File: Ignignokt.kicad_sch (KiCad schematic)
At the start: 270 parts, among them J1 Barrel_Jack_Switch, J2 Conn_01x02_Pin, Q1 IRLB8721PBF, Q2 FQP27P06, U1 LM2585S-12, U2 LM2937ET-5.0, U3 PIC12F675-IMC

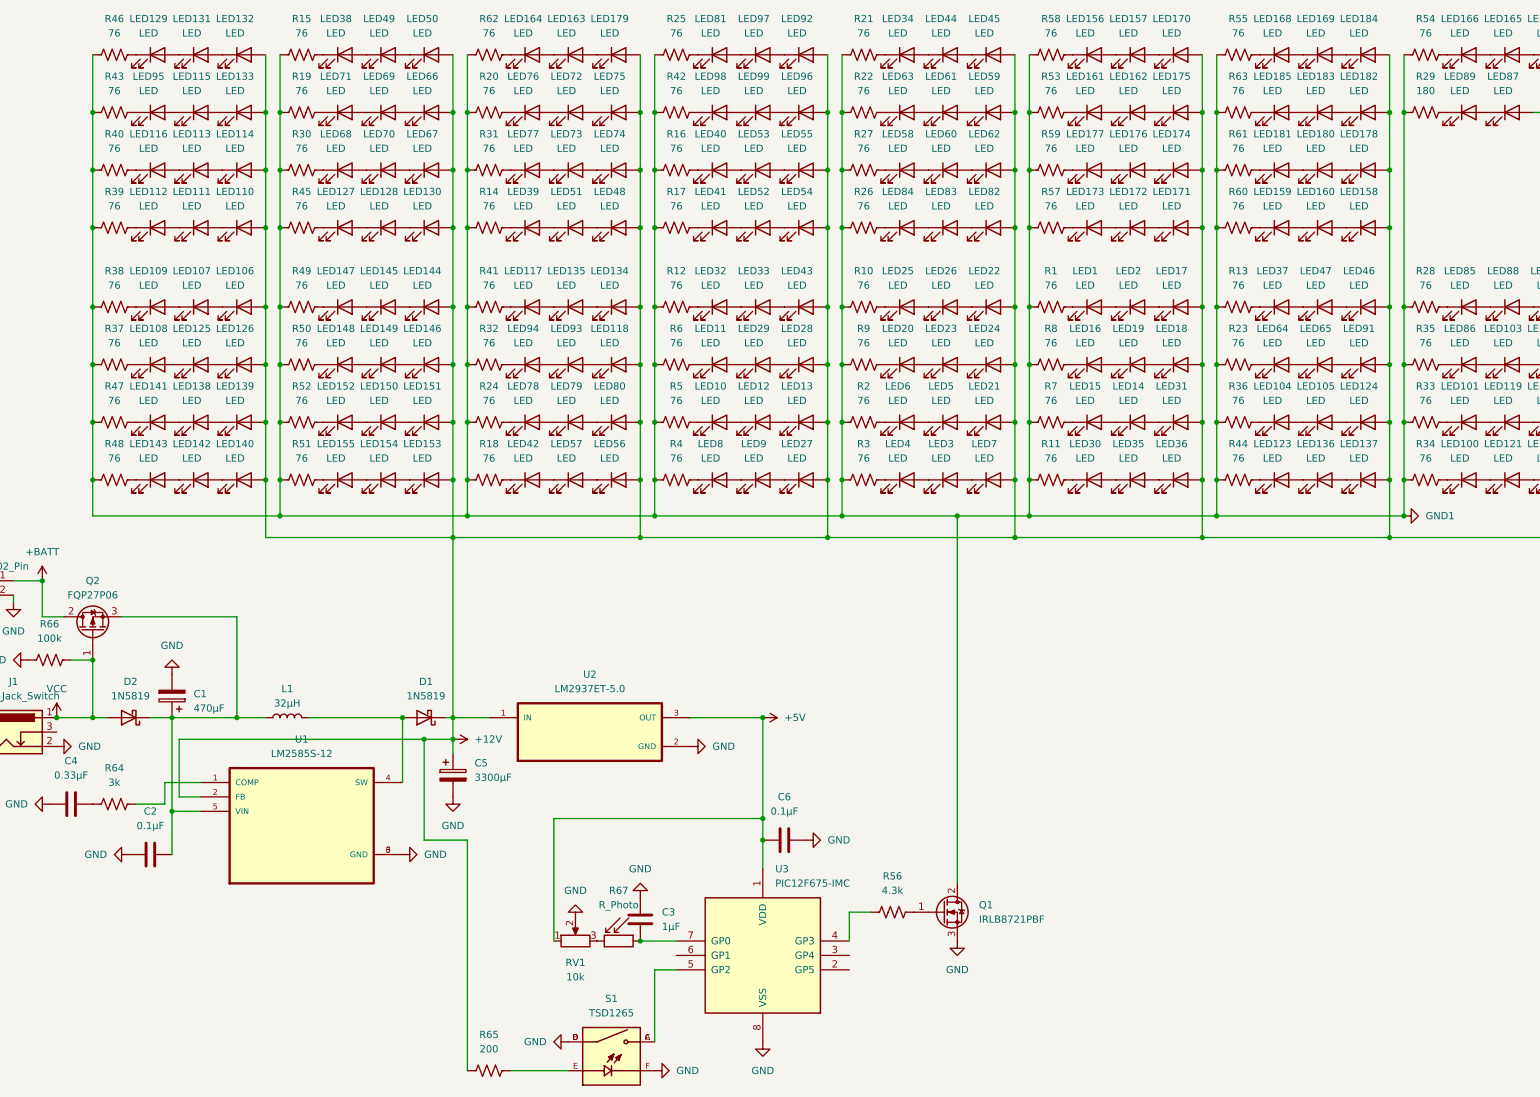
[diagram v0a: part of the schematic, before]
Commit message: Small tweaks to board
The MOSFET for the LEDs was a TO-247 which did not match the part I had selected. Changed it to a TO-220 to match the part. Also added a pull-down resistor to the gate to ensure it turns off when there is no longer a voltage on the pin. The PIC chip will ground it but it makes sense to have the extra part in case the board is used without it.

Signed-off-by: Nathan Hjelm <hjelmn@me.com>
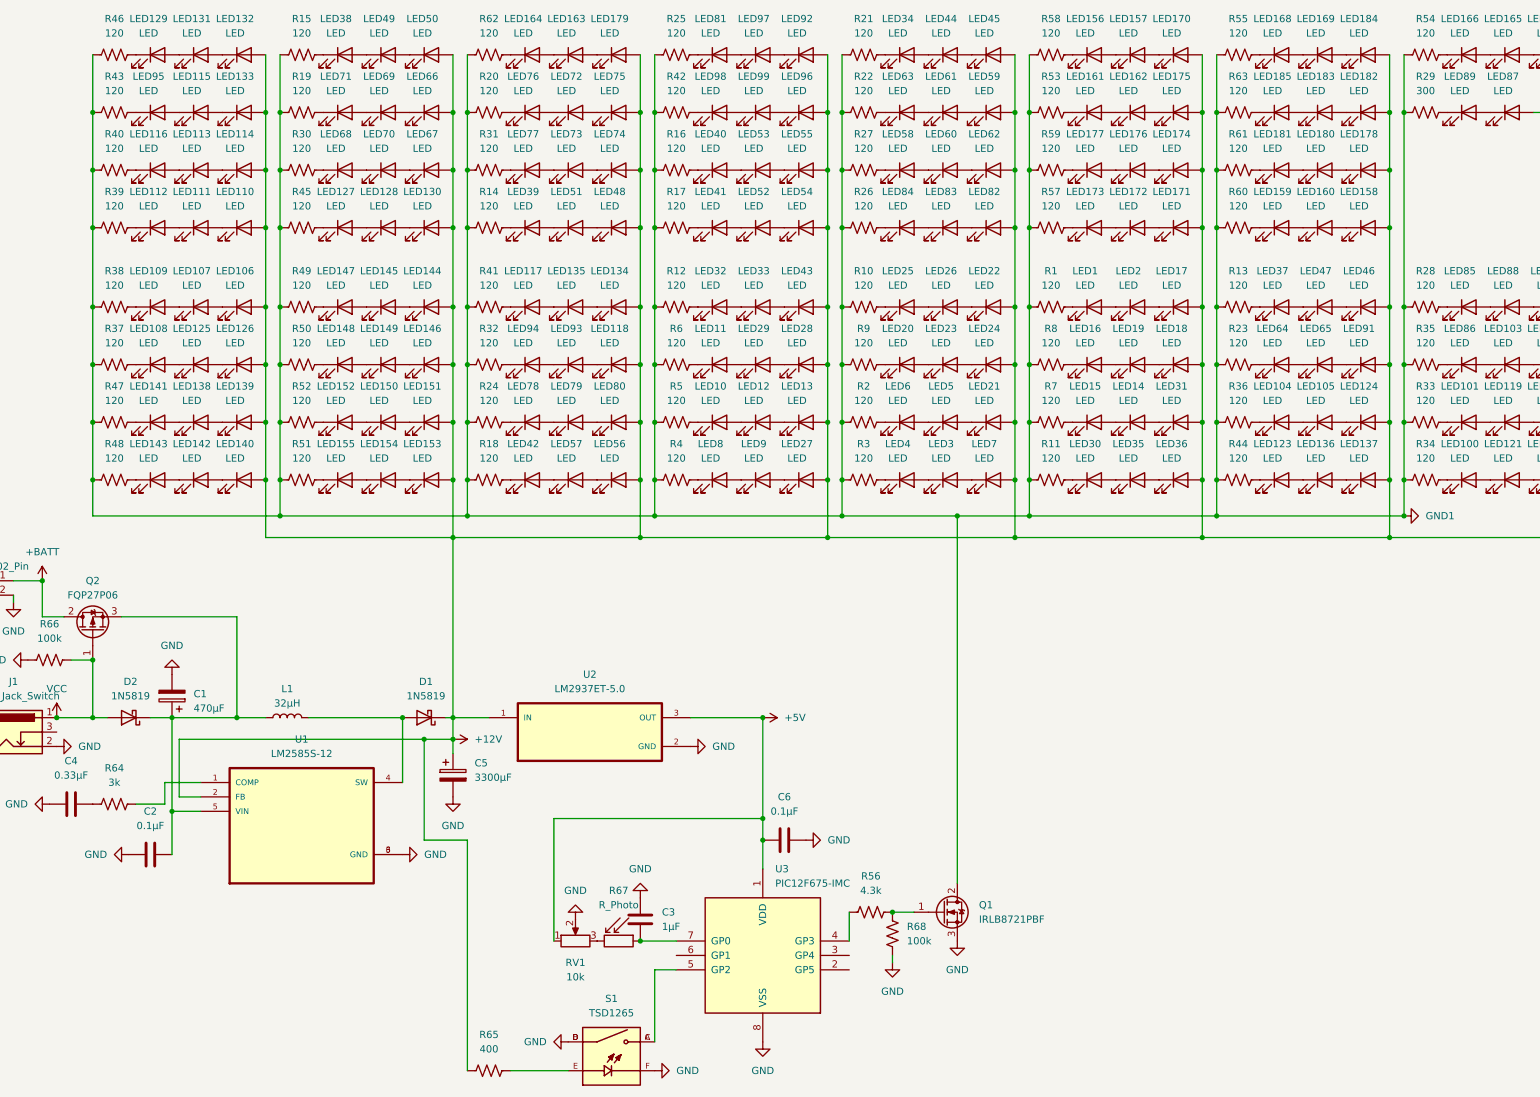
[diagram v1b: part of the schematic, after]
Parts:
- added R68: 100k, Resistor_THT:R_Axial_DIN0207_L6.3mm_D2.5mm_P10.16mm_Horizontal, symbol Device:R_US
- Q1: footprint Package_TO_SOT_THT:TO-247-3_Vertical -> Package_TO_SOT_THT:TO-220-3_Vertical
- R1, R10, R11, R12, R13, R14, R15, R16, R17, R18, R19, R2, R20, R21, R22, R23, R24, R25, R26, R27, R28, R3, R30, R31, R32, R33, R34, R35, R36, R37, R38, R39, R4, R40, R41, R42, R43, R44, R45, R46, R47, R48, R49, R5, R50, R51, R52, R53, R54, R55, R57, R58, R59, R6, R60, R61, R62, R63, R7, R8, R9: value 76 -> 120
- R29: value 180 -> 300
- R65: value 200 -> 400
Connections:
- net GND: now also R68.2
- net at Q1.1 (G), R56.1: now also R68.1
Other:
- moved on the sheet: R56

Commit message: Small tweaks
The original schematic I used to design the board erroneously used pin 4 (GPIO3) as an output pin. This will not work with a PIC2F675 as that pin is input-only. Moved the output to GPIO4 to correct the issue and adjusted some other components based on observations.

To fix the boards I have I put a jumper between GPIO3 and GPIO4 and disabled external MCLR to avoid the output causing a reset of the chip.

Also, can use a 200 ohm resistor in place of the potentiometer (dropped to 1k). 10k might be a bit too high but could work as well. Will do more calculations to see what is best since the 10k can only go down to 5.3k. At 200 ohm it takes about 8 clock cycles for the GPIO pin to register high at the appropriate light level.

Signed-off-by: Nathan Hjelm <hjelmn@me.com>
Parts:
- removed R68: 100k, Resistor_THT:R_Axial_DIN0207_L6.3mm_D2.5mm_P10.16mm_Horizontal, symbol Device:R_US
- added C7: 1µF, Capacitor_THT:C_Disc_D5.1mm_W3.2mm_P5.00mm, symbol Device:C
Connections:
- net GND: now also C7.2
- net at U3.3 (GP4): now also R56.2
- net at U3.4 (GP3): no longer R56.2
- net at S1.A, S1.C, U3.5 (GP2): now also C7.1
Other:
- moved on the sheet: R56
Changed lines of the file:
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@@
   (junction (at 284.48 66.04) (diameter 0) (color 0 0 0 0)
   )
-  (junction (at 194.31 172.72) (diameter 0) (color 0 0 0 0)
-  )
   (junction (at 182.88 41.91) (diameter 0) (color 0 0 0 0)
   )
@@
   (junction (at 67.31 154.94) (diameter 0) (color 0 0 0 0)
   )
+  (junction (at 152.4 182.88) (diameter 0) (color 0 0 0 0)
+  )
   (junction (at 314.96 31.75) (diameter 0) (color 0 0 0 0)
   )
@@
     (stroke (width 0) (type default))
   )
-  (wire (pts (xy 186.69 172.72) (xy 186.69 177.8))
-    (stroke (width 0) (type default))
-  )
   (wire (pts (xy 205.74 102.87) (xy 185.42 102.87))
     (stroke (width 0) (type default))
@@
     (stroke (width 0) (type default))
   )
+  (wire (pts (xy 186.69 180.34) (xy 189.23 180.34))
+    (stroke (width 0) (type default))
+  )
   (wire (pts (xy 119.38 86.36) (xy 119.38 96.52))
     (stroke (width 0) (type default))
@@
     (stroke (width 0) (type default))
   )
-  (wire (pts (xy 194.31 172.72) (xy 198.12 172.72))
+  (wire (pts (xy 189.23 172.72) (xy 198.12 172.72))
     (stroke (width 0) (type default))
   )
@@
     (stroke (width 0) (type default))
   )
-  (wire (pts (xy 194.31 180.34) (xy 194.31 181.61))
-    (stroke (width 0) (type default))
-  )
   (wire (pts (xy 156.21 182.88) (xy 152.4 182.88))
     (stroke (width 0) (type default))
@@
     )
   )
+  (symbol (lib_id "Device:C") (at 148.59 182.88 270) (unit 1)
+    (in_bom yes) (on_board yes) (dnp no) (fields_autoplaced)
+    (property "Reference" "C7" (at 148.59 175.26 90)
+      (effects (font (size 1.27 1.27)))
+    )
+    (property "Value" "1µF" (at 148.59 177.8 90)
+      (effects (font (size 1.27 1.27)))
+    )
+    (property "Footprint" "Capacitor_THT:C_Disc_D5.1mm_W3.2mm_P5.00mm" (at 144.78 183.8452 0)
+      (effects (font (size 1.27 1.27)) hide)
+    )
+    (property "Datasheet" "~" (at 148.59 182.88 0)
+      (effects (font (size 1.27 1.27)) hide)
+    )
+    (pin "2")
+    (pin "1")
+    (instances
+      (project "Ignignokt"
+        (path "/f0a33db0-88ba-4d3e-9175-b5a39f1c39d8"
+          (reference "C7") (unit 1)
+        )
+      )
+    )
+  )
   (symbol (lib_id "Device:R_US") (at 156.21 31.75 270) (unit 1)
     (in_bom yes) (on_board yes) (dnp no) (fields_autoplaced)
@@
     )
   )
-  (symbol (lib_id "Device:R_US") (at 194.31 176.53 0) (unit 1)
-    (in_bom yes) (on_board yes) (dnp no) (fields_autoplaced)
-    (property "Reference" "R68" (at 196.85 175.26 0)
-      (effects (font (size 1.27 1.27)) (justify left))
-    )
-    (property "Value" "100k" (at 196.85 177.8 0)
-      (effects (font (size 1.27 1.27)) (justify left))
-    )
-    (property "Footprint" "Resistor_THT:R_Axial_DIN0207_L6.3mm_D2.5mm_P10.16mm_Horizontal" (at 195.326 176.784 90)
-      (effects (font (size 1.27 1.27)) hide)
-    )
-    (property "Datasheet" "~" (at 194.31 176.53 0)
-      (effects (font (size 1.27 1.27)) hide)
-    )
-    (pin "1")
-    (pin "2")
-    (instances
-      (project "Ignignokt"
-        (path "/f0a33db0-88ba-4d3e-9175-b5a39f1c39d8"
-          (reference "R68") (unit 1)
-        )
-      )
-    )
-  )
   (symbol (lib_id "Device:LED") (at 212.09 66.04 0) (unit 1)
     (in_bom yes) (on_board yes) (dnp no) (fields_autoplaced)
@@
     )
   )
-  (symbol (lib_id "power:GND") (at 194.31 181.61 0) (unit 1)
-    (in_bom yes) (on_board yes) (dnp no) (fields_autoplaced)
-    (property "Reference" "#PWR022" (at 194.31 187.96 0)
-      (effects (font (size 1.27 1.27)) hide)
-    )
-    (property "Value" "GND" (at 194.31 186.69 0)
-      (effects (font (size 1.27 1.27)))
-    )
-    (property "Footprint" "" (at 194.31 181.61 0)
-      (effects (font (size 1.27 1.27)) hide)
-    )
-    (property "Datasheet" "" (at 194.31 181.61 0)
-      (effects (font (size 1.27 1.27)) hide)
-    )
-    (pin "1")
-    (instances
-      (project "Ignignokt"
-        (path "/f0a33db0-88ba-4d3e-9175-b5a39f1c39d8"
-          (reference "#PWR022") (unit 1)
-        )
-      )
-    )
-  )
   (symbol (lib_id "Device:R_US") (at 222.25 31.75 270) (unit 1)
     (in_bom yes) (on_board yes) (dnp no) (fields_autoplaced)
@@
     )
   )
-  (symbol (lib_id "Device:R_US") (at 190.5 172.72 270) (unit 1)
+  (symbol (lib_id "Device:R_US") (at 189.23 176.53 0) (unit 1)
     (in_bom yes) (on_board yes) (dnp no) (fields_autoplaced)
-    (property "Reference" "R56" (at 190.5 166.37 90)
-      (effects (font (size 1.27 1.27)))
+    (property "Reference" "R56" (at 191.77 175.26 0)
+      (effects (font (size 1.27 1.27)) (justify left))
     )
-    (property "Value" "4.3k" (at 190.5 168.91 90)
-      (effects (font (size 1.27 1.27)))
+    (property "Value" "4.3k" (at 191.77 177.8 0)
+      (effects (font (size 1.27 1.27)) (justify left))
     )
-    (property "Footprint" "Resistor_THT:R_Axial_DIN0207_L6.3mm_D2.5mm_P10.16mm_Horizontal" (at 190.246 173.736 90)
+    (property "Footprint" "Resistor_THT:R_Axial_DIN0207_L6.3mm_D2.5mm_P10.16mm_Horizontal" (at 190.246 176.784 90)
       (effects (font (size 1.27 1.27)) hide)
     )
-    (property "Datasheet" "~" (at 190.5 172.72 0)
+    (property "Datasheet" "~" (at 189.23 176.53 0)
       (effects (font (size 1.27 1.27)) hide)
     )
@@
         )
       )
+    )
+  )
+  (symbol (lib_id "power:GND") (at 144.78 182.88 270) (unit 1)
+    (in_bom yes) (on_board yes) (dnp no) (fields_autoplaced)
+    (property "Reference" "#PWR023" (at 138.43 182.88 0)
+      (effects (font (size 1.27 1.27)) hide)
+    )
+    (property "Value" "GND" (at 140.97 182.88 90)
+      (effects (font (size 1.27 1.27)) (justify right))
+    )
+    (property "Footprint" "" (at 144.78 182.88 0)
+      (effects (font (size 1.27 1.27)) hide)
+    )
+    (property "Datasheet" "" (at 144.78 182.88 0)
+      (effects (font (size 1.27 1.27)) hide)
+    )
+    (pin "1")
+    (instances
+      (project "Ignignokt"
+        (path "/f0a33db0-88ba-4d3e-9175-b5a39f1c39d8"
+          (reference "#PWR023") (unit 1)
+        )
+      )

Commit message: Update with a 4:0 LEDs:resistors ratio
After closer inspection it seems the original sign was using a 4:1 ratio given there are 3 resistors for each eye/eyebrow (12 LEDS), 3 for the right arm (12 LEDs), etc. The LEDs I ordered also appear to be 2.6-2.9v forward voltage drop (not the 3-3.2 advetised) so it is better to do 4 LEDs to one 64 ohm resistor to get ~ 10mA of current. These LEDs are super bright so running close to 20mA would be a mistake.

Signed-off-by: Nathan Hjelm <hjelmn@me.com>
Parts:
- removed R11, R14, R17, R18, R22, R3, R35, R37, R4, R46, R48, R51, R55, R59: 120, Resistor_THT:R_Axial_DIN0207_L6.3mm_D2.5mm_P10.16mm_Horizontal, symbol Device:R_US
- removed R29: 300, Resistor_THT:R_Axial_DIN0207_L6.3mm_D2.5mm_P10.16mm_Horizontal, symbol Device:R_US
- added RV1: 1k, Potentiometer_THT:Potentiometer_Bourns_3299W_Vertical, symbol Device:R_Potentiometer
- C5: footprint Capacitor_THT:CP_Radial_D12.5mm_P5.00mm -> Capacitor_THT:CP_Radial_D18.0mm_P7.50mm
- R1, R2: value 120 -> 76
- R10: renamed from R13; value 120 -> 76
- R11: renamed from R15; value 120 -> 76
- R12: renamed from R16; value 120 -> 76
- R13: renamed from R23; value 120 -> 76
- R14: renamed from R30; value 120 -> 76
- R15: renamed from R19; value 120 -> 76
- R16: renamed from R20; value 120 -> 76
- R17: renamed from R31; value 120 -> 76
- R18: renamed from R24; value 120 -> 76
- R19: renamed from R27; value 120 -> 76
- R20: renamed from R21; value 120 -> 340
- R21: renamed from R25; value 120 -> 76
- R22: renamed from R26; value 120 -> 76
- R23: renamed from R28; value 120 -> 76
- R24: renamed from R36; value 120 -> 76
- R25: renamed from R32; value 120 -> 76
- R26: renamed from R34; value 120 -> 76
- R27: renamed from R33; value 120 -> 76
- R28: renamed from R45; value 120 -> 76
- R29: renamed from R38; value 120 -> 76
- R3: renamed from R10; value 120 -> 76
- R30: renamed from R39; value 120 -> 76
- R31: renamed from R42; value 120 -> 76
- R32: renamed from R44; value 120 -> 76
- R33: renamed from R43; value 120 -> 76
- R34: renamed from R40; value 120 -> 76
- R35: renamed from R41; value 120 -> 76
- R36: renamed from R47; value 120 -> 76
- R37: renamed from R49; value 120 -> 76
- R38: renamed from R50; value 120 -> 76
- R39: renamed from R52; value 120 -> 76
- R4: renamed from R5; value 120 -> 76
- R40: renamed from R53; value 120 -> 340
- R41: renamed from R60; value 120 -> 76
- R42: renamed from R54; value 120 -> 76
- R43: renamed from R62; value 120 -> 340
- R45: renamed from R57; value 120 -> 76
- R46: renamed from R58; value 120 -> 76
- R47: renamed from R63; value 120 -> 76
- R48: renamed from R61; value 120 -> 76
- R5: renamed from R6; value 120 -> 76
- R50: renamed from R65; value 400 -> 200
- R6: renamed from R7; value 120 -> 76
- R7: renamed from R8; value 120 -> 76
- R8: renamed from R9; value 120 -> 76
- R9: renamed from R12; value 120 -> 76
- RV2: renamed from RV1; value 10k -> 1k
- renumbered C7 to C6, C6 to C7, LED102 to LED100, LED103 to LED102, LED100 to LED103, LED107 to LED106, LED106 to LED107, LED110 to LED109, LED13 to LED11, LED109 to LED110, LED118 to LED117, LED117 to LED118, LED120 to LED119, LED11 to LED12, LED119 to LED120, LED122 to LED121, LED121 to LED122, LED124 to LED123, LED123 to LED124, LED126 to LED125, LED125 to LED126, LED128 to LED127, LED127 to LED128, LED12 to LED13, LED132 to LED131, LED131 to LED132, LED137 to LED136, LED136 to LED137, LED143 to LED142, LED142 to LED143, LED147 to LED146, LED146 to LED147, LED149 to LED148, LED148 to LED149, LED16 to LED15, LED160 to LED158, LED15 to LED16, LED158 to LED160, LED164 to LED163, LED163 to LED164, LED19 to LED17, LED172 to LED170, LED170 to LED172, LED177 to LED176, LED176 to LED177, LED179 to LED178, LED178 to LED179, LED183 to LED182, LED182 to LED183, LED185 to LED184, LED184 to LED185, LED17 to LED19, LED21 to LED20, LED20 to LED21, LED23 to LED22, LED22 to LED23, LED26 to LED25, LED25 to LED26, LED29 to LED28, LED28 to LED29, LED37 to LED36, LED36 to LED37, LED39 to LED38, LED38 to LED39, LED43 to LED42, LED42 to LED43, LED47 to LED46, LED46 to LED47, LED50 to LED48, LED48 to LED50, LED54 to LED53, LED55 to LED54, LED53 to LED55, LED57 to LED56, LED56 to LED57, LED61 to LED59, LED7 to LED6, LED59 to LED60, LED62 to LED61, LED60 to LED62, LED65 to LED64, LED64 to LED65, LED69 to LED68, LED68 to LED69, LED6 to LED7, LED75 to LED72, LED72 to LED73, LED73 to LED75, LED79 to LED78, LED78 to LED79, LED9 to LED8, LED82 to LED81, LED81 to LED82, LED84 to LED83, LED83 to LED84, LED86 to LED85, LED85 to LED86, LED89 to LED87, LED87 to LED89, LED8 to LED9, LED95 to LED93, LED93 to LED94, LED94 to LED95, LED99 to LED96, LED96 to LED97, LED97 to LED98, LED98 to LED99, R56 to R44, R64 to R49, R66 to R51, R67 to R52
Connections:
- net +12V: now also RV1.1; no longer LED100.2 (A), LED107.2 (A), LED109.2 (A), LED11.2 (A), LED114.2 (A), LED117.2 (A), LED119.2 (A), LED121.2 (A), LED123.2 (A), LED125.2 (A), LED130.2 (A), LED131.2 (A), LED133.2 (A), LED134.2 (A), LED136.2 (A), LED139.2 (A), LED140.2 (A), LED144.2 (A), LED147.2 (A), LED151.2 (A), LED153.2 (A), LED160.2 (A), LED167.2 (A), LED171.2 (A), LED172.2 (A), LED174.2 (A), LED175.2 (A), LED178.2 (A), LED179.2 (A), LED18.2 (A), LED183.2 (A), LED185.2 (A), LED19.2 (A), LED20.2 (A), LED23.2 (A), LED24.2 (A), LED27.2 (A), LED29.2 (A), LED31.2 (A), LED37.2 (A), LED42.2 (A), LED45.2 (A), LED47.2 (A), LED48.2 (A), LED50.2 (A), LED53.2 (A), LED54.2 (A), LED57.2 (A), LED6.2 (A), LED60.2 (A), LED61.2 (A), LED66.2 (A), LED67.2 (A), LED72.2 (A), LED74.2 (A), LED80.2 (A), LED81.2 (A), LED89.2 (A), LED90.2 (A), LED91.2 (A), LED92.2 (A), LED97.2 (A), R50.2
- net +5V: now also R50.2
- net GND: now also RV1.2
- net GND1: now also LED21.1 (K), LED22.2 (A)
- net at LED123.1 (K): now also R32.1; no longer LED105.2 (A)
- net at LED19.1 (K): now also LED18.2 (A); no longer LED2.2 (A)
- net at LED156.1 (K): now also LED160.2 (A); no longer R46.1
- net at LED156.2 (A): now also LED105.2 (A), LED107.2 (A), LED11.2 (A), LED111.2 (A), LED118.2 (A), LED119.2 (A), LED121.2 (A), LED128.2 (A), LED131.2 (A), LED132.2 (A), LED136.2 (A), LED139.2 (A), LED143.2 (A), LED146.2 (A), LED151.2 (A), LED154.2 (A), LED157.2 (A), LED168.2 (A), LED169.2 (A), LED175.2 (A), LED176.2 (A), LED178.2 (A), LED179.2 (A), LED19.2 (A), LED2.2 (A), LED20.2 (A), LED21.2 (A), LED25.2 (A), LED30.2 (A), LED32.2 (A), LED45.2 (A), LED46.2 (A), LED48.2 (A), LED54.2 (A), LED56.2 (A), LED63.2 (A), LED67.2 (A), LED68.2 (A), LED73.2 (A), LED77.2 (A), LED80.2 (A), LED81.2 (A), LED85.2 (A), LED91.2 (A), LED92.2 (A), LED97.2 (A), RV1.3; no longer LED157.1 (K)
- net at LED41.1 (K): now also R12.1
- net at LED41.2 (A): now also LED40.1 (K); no longer LED52.1 (K)
- net at LED63.1 (K): now also LED59.2 (A)
- net at LED100.1 (K): now also R27.1; no longer LED102.2 (A)
- net at LED24.1 (K): now also LED23.2 (A); no longer LED22.2 (A)
- net at LED8.1 (K): now also R3.1; no longer LED9.2 (A)
- net at LED145.1 (K): now also R37.1; no longer LED146.2 (A)
- net at LED101.1 (K): now also LED100.2 (A); no longer R27.1
- net at LED66.1 (K): now also LED50.2 (A); no longer LED68.2 (A)
- net at R18.1: now also LED57.1 (K); no longer LED79.1 (K)
- net at R8.1: now also LED23.1 (K); no longer LED21.1 (K)
- net at LED22.1 (K): now also LED24.2 (A); no longer LED21.2 (A)
- net at R17.1: now also LED72.1 (K); no longer LED77.1 (K)
- net at R9.1: now also LED33.1 (K); no longer LED32.1 (K)
- net at LED82.1 (K): now also LED83.2 (A); no longer R21.1
- net at LED108.1 (K): now also R28.1
- net at LED146.1 (K): now also LED147.2 (A); no longer R37.1
- net at LED131.1 (K): now also LED133.2 (A); no longer LED132.2 (A)
- net at LED124.1 (K): now also LED123.2 (A); no longer R32.1
- net at LED135.1 (K): now also R35.1; no longer LED118.2 (A)
- net at LED128.1 (K): now also LED125.2 (A); no longer R28.1
- net at LED127.1 (K): now also R33.1; no longer LED128.2 (A)
- net at LED85.1 (K): now also LED90.2 (A)
- net at LED102.1 (K): now also R26.1; no longer LED85.2 (A)
- net at LED51.1 (K): now also R15.1; no longer LED38.2 (A)
- net at LED140.1 (K): now also R36.1; no longer LED143.2 (A)
- net at LED182.1 (K): now also R47.1; no longer LED184.2 (A)
- net at LED182.2 (A): now also LED184.1 (K); no longer LED183.1 (K)
- net at R31.1: now also LED93.1 (K); no longer LED99.1 (K)
- net at LED169.1 (K): now also LED185.2 (A); no longer LED168.2 (A)
- net at LED185.1 (K): now also LED184.2 (A); no longer LED169.2 (A)
- net at LED59.1 (K): now also LED62.2 (A); no longer LED63.2 (A)
- net at LED60.1 (K): now also LED61.2 (A); no longer LED59.2 (A)
- net at LED30.1 (K): now also LED31.2 (A)
- net at LED103.1 (K): now also LED102.2 (A); no longer R26.1
- net at LED26.1 (K): now also LED27.2 (A); no longer R3.1
- net at LED71.1 (K): now also R14.1; no longer R15.1
- net at LED68.1 (K): now also LED66.2 (A); no longer LED71.2 (A)
- net at LED3.1 (K): now also R1.1; no longer LED4.2 (A)
- net at LED3.2 (A): now also LED4.1 (K); no longer LED6.1 (K)
- net at LED87.1 (K): now also R24.1
- net at LED1.1 (K): now also LED4.2 (A); no longer R1.1
- net at LED9.1 (K): now also R4.1
- net at LED47.1 (K): now also R13.1; no longer LED46.2 (A)
- net at LED75.1 (K): now also LED74.2 (A); no longer LED77.2 (A)
- net at LED75.2 (A): now also LED77.1 (K); no longer LED74.1 (K)
- net at LED168.1 (K): now also LED167.2 (A)
- net at LED113.1 (K): now also R30.1; no longer LED116.2 (A)
- net at LED115.1 (K): now also LED116.2 (A); no longer LED93.2 (A)
- net at R22.1: now also LED61.1 (K); no longer LED83.1 (K)
- net at LED173.2 (A): now also LED174.1 (K); no longer LED170.1 (K)
- net at LED38.1 (K): now also R11.1
- net at LED153.1 (K): now also R39.1; no longer LED154.2 (A)
- net at LED181.1 (K): now also LED183.2 (A); no longer R48.1
- net at LED141.1 (K): now also LED140.2 (A); no longer R36.1
- net at LED118.1 (K): now also LED117.2 (A); no longer R35.1
- net at LED177.2 (A): now also LED176.1 (K); no longer LED174.1 (K)
- net at LED65.1 (K): now also LED47.2 (A); no longer R13.1
- net at LED39.1 (K): now also LED38.2 (A); no longer R11.1
- net at LED109.1 (K): now also R29.1; no longer LED111.2 (A)
- net at LED84.1 (K): now also LED60.2 (A); no longer LED83.2 (A)
- net at LED155.1 (K): now also LED134.2 (A)
- net at LED104.1 (K): now also LED89.2 (A); no longer R24.1
- net at LED76.1 (K): now also LED53.2 (A); no longer R16.1
- net at LED112.1 (K): now also LED114.2 (A); no longer R30.1
- net at LED7.1 (K): now also LED6.2 (A); no longer R2.1
- net at LED43.1 (K): now also LED42.2 (A)
- net at LED10.1 (K): now also LED9.2 (A); no longer R4.1
- net at LED172.1 (K): now also LED171.2 (A); no longer LED157.2 (A)
- net at LED177.1 (K): now also LED174.2 (A); no longer LED176.2 (A)
- net at LED35.1 (K): now also R10.1; no longer LED30.2 (A)
- net at LED110.1 (K): now also LED109.2 (A); no longer R29.1
- net at LED36.1 (K): now also LED37.2 (A); no longer R10.1
- net at LED129.1 (K): now also LED130.2 (A)
- net at LED152.1 (K): now also LED153.2 (A); no longer R39.1
- net at LED142.1 (K): now also LED144.2 (A)
- net at LED69.1 (K): now also LED71.2 (A); no longer R14.1
- new net: LED57.2 (A), LED79.1 (K)
- new net: LED72.2 (A), LED74.1 (K)
- new net: LED29.2 (A), LED32.1 (K)
- new net: LED170.1 (K), R46.1
- new net: LED6.1 (K), R2.1
- new net: LED83.1 (K), R21.1
- new net: LED52.1 (K), R16.1
- new net: LED157.1 (K), LED172.2 (A)
- new net: LED93.2 (A), LED99.1 (K)
- new net: LED183.1 (K), R48.1
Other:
- note added: "Ignignokt"
- note added: "v0.2"
- moved on the sheet: C1, C2, C3, C4, C5, C6, C7, D1, D2, J1, J2, L1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

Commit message: Small tweaks
Signed-off-by: Nathan Hjelm <hjelmn@me.com>
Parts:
- Q1, Q2: footprint Package_TO_SOT_THT:TO-220-3_Vertical -> Package_TO_SOT_THT:TO-220-3_Horizontal_TabDown
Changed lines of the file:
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@@
       (effects (font (size 1.27 1.27)) (justify left))
     )
-    (property "Footprint" "Package_TO_SOT_THT:TO-220-3_Vertical" (at 209.55 175.895 0)
+    (property "Footprint" "Package_TO_SOT_THT:TO-220-3_Horizontal_TabDown" (at 209.55 175.895 0)
       (effects (font (size 1.27 1.27) italic) (justify left) hide)
     )
@@
       (effects (font (size 1.27 1.27)))
     )
-    (property "Footprint" "Package_TO_SOT_THT:TO-220-3_Vertical" (at 56.515 124.46 0)
+    (property "Footprint" "Package_TO_SOT_THT:TO-220-3_Horizontal_TabDown" (at 56.515 124.46 0)
       (effects (font (size 1.27 1.27) italic) (justify left) hide)
     )

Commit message: Fix a minor issue
Signed-off-by: Nathan Hjelm <hjelmn@me.com>
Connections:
- net GND1: no longer LED21.1 (K), LED22.2 (A)
- new net: LED21.1 (K), LED22.2 (A)
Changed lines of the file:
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@@
   (junction (at 257.81 34.29) (diameter 0) (color 0 0 0 0)
   )
-  (junction (at 207.01 105.41) (diameter 0) (color 0 0 0 0)
-  )
   (junction (at 95.25 38.1) (diameter 0) (color 0 0 0 0)
   )
@@
     (stroke (width 0) (type default))
   )
-  (wire (pts (xy 207.01 105.41) (xy 207.01 109.22))
-    (stroke (width 0) (type default))
-  )
